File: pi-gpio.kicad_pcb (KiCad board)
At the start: 2 copper layers, 65.1 x 30.1 mm, 15 parts, among them J1 Raspberry_Pi_2_3, J2 printerRelay, J3 UART, J4 uartPower, J5 adxl, J6 powerIn

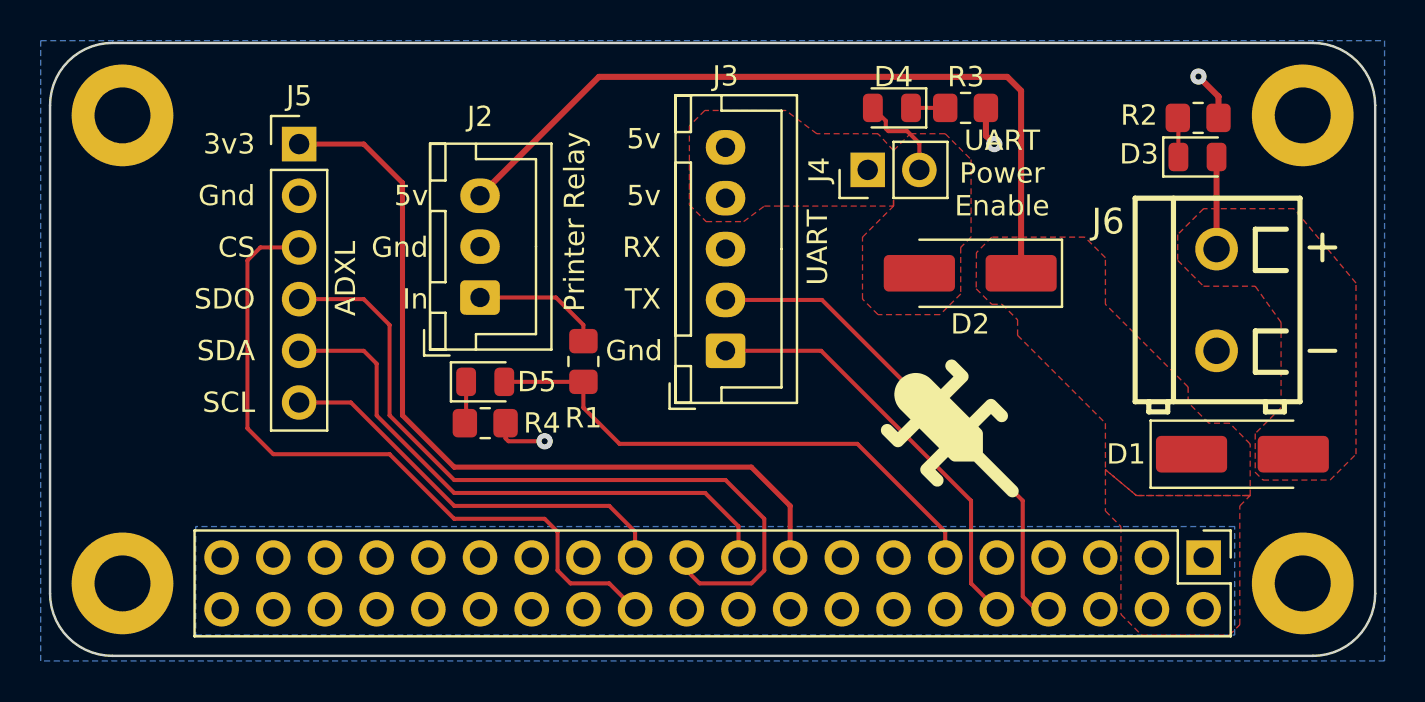
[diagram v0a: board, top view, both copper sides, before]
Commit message: Doubled SPI headers, added I2C
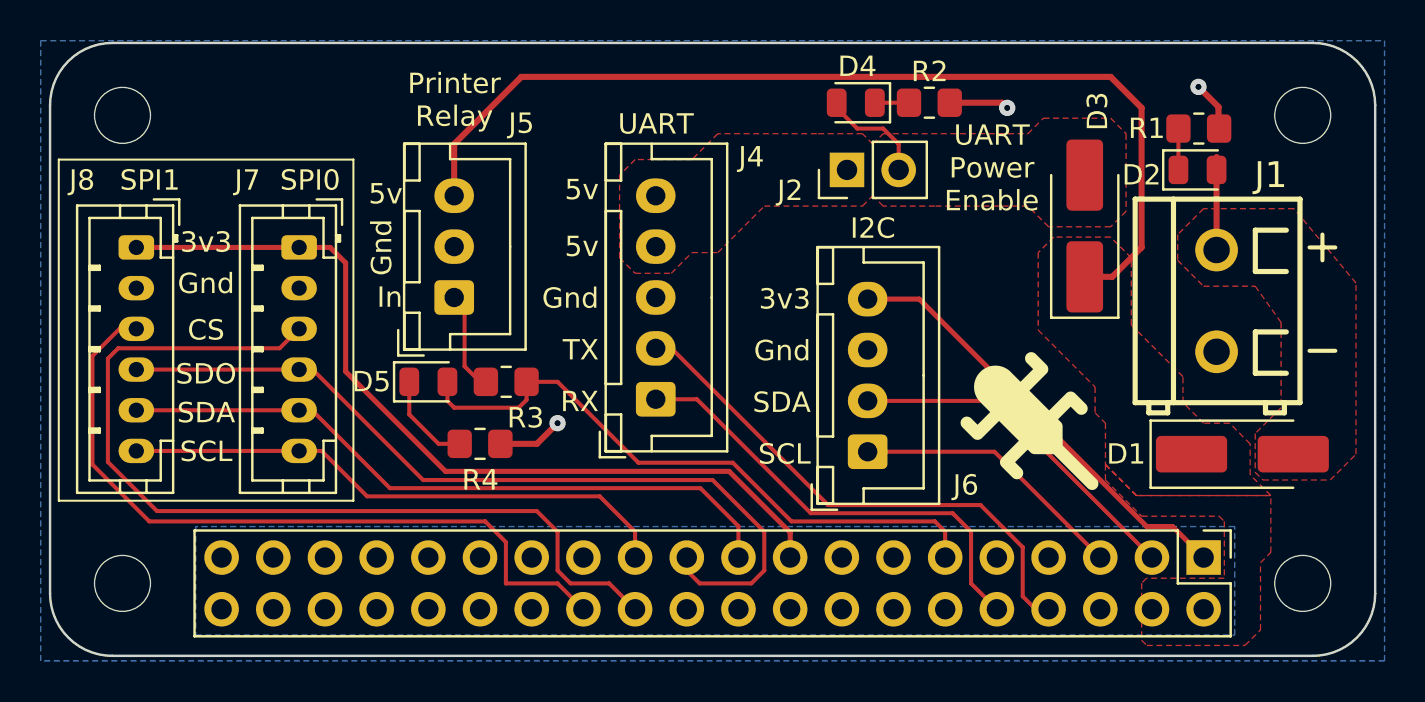
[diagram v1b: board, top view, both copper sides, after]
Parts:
- added J7: SPI0, Connector_JST:JST_PH_B6B-PH-K_1x06_P2.00mm_Vertical, F.Cu at (64.8, 35.6)
- added J8: SPI1, Connector_JST:JST_PH_B6B-PH-K_1x06_P2.00mm_Vertical, F.Cu at (56.8, 35.6)
- D2: value B340A-13-F -> Red; footprint Diode_SMD:D_SMA_Handsoldering -> LED_SMD:LED_0805_2012Metric
- D3: value Red -> B340A-13-F; footprint LED_SMD:LED_0805_2012Metric -> Diode_SMD:D_SMA_Handsoldering
- J1: value Raspberry_Pi_2_3 -> powerIn; footprint jacob-libs:RaspberryPi_Zero_BoardLayout -> jacob-libs:TerminalBlock_MAX_MX127-5.0-02P_1x02_P5.00mm; moved to F.Cu
- J2: value printerRelay -> uartPower; footprint Connector_JST:JST_XH_B3B-XH-A_1x03_P2.50mm_Vertical -> Connector_PinHeader_2.54mm:PinHeader_1x02_P2.54mm_Vertical
- J3: value UART -> Raspberry_Pi_2_3; footprint Connector_JST:JST_XH_B5B-XH-A_1x05_P2.50mm_Vertical -> jacob-libs:RaspberryPi_Zero_BoardLayout; moved to B.Cu
- J4: value uartPower -> UART; footprint Connector_PinHeader_2.54mm:PinHeader_1x02_P2.54mm_Vertical -> Connector_JST:JST_XH_B5B-XH-A_1x05_P2.50mm_Vertical
- J5: value adxl -> printerRelay; footprint Connector_PinHeader_2.54mm:PinHeader_1x06_P2.54mm_Vertical -> Connector_JST:JST_XH_B3B-XH-A_1x03_P2.50mm_Vertical
- J6: value powerIn -> i2c; footprint jacob-libs:TerminalBlock_MAX_MX127-5.0-02P_1x02_P5.00mm -> Connector_JST:JST_XH_B4B-XH-A_1x04_P2.50mm_Vertical
- R1: value 1K -> 150R
- R3: value 150R -> 1K
- moved R1 32.3 mm to (109.0, 29.7), turned to 0 degrees
- moved R3 26.3 mm to (74.9, 42.2)
- moved J3 25.6 mm to (109.2, 50.8)
- moved J2 19.1 mm to (91.7, 31.8)
- moved J6 18.7 mm to (92.7, 45.6)
- moved J4 15.3 mm to (82.3, 43.0)
- moved R2 13.2 mm to (95.7, 28.4)
- moved J1 12.6 mm to (109.9, 38.2)
- moved D2 12.3 mm to (108.9, 31.8), turned to 0 degrees
- moved J5 10.7 mm to (72.4, 38.0), turned to 90 degrees
- moved D3 6.49 mm to (103.4, 34.5), turned to 90 degrees
- moved D5 2.79 mm to (71.1, 42.2)
- moved D4 1.80 mm to (92.1, 28.4)
- moved R4 1.05 mm to (73.7, 45.2)
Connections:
- D2 pad 1: +5V -> Net-(D2-K)
- D2 pad 2: Net-(D2-A) -> Net-(D1-A)
- D3 pad 1: Net-(D3-K) -> +5V
- D3 pad 2: Net-(D1-A) -> Net-(D3-A)
- D4 pad 2: Net-(D2-A) -> Net-(D3-A)
- J1 pad 1: +3V3 -> GND
- J1 pad 2: +5V -> Net-(D1-A)
- J2 pad 2: GND -> Net-(D3-A)
- J3 pad 1: /UART_RXD -> +3V3
- J3 pad 2: /UART_TXD -> +5V
- J3 pad 3: GND -> /I2C_SDA
- J3 pad 4: Net-(J3-Pin_4) -> +5V
- J3 pad 5: Net-(J3-Pin_4) -> /I2C_SCL
- J4 pad 1: Net-(J3-Pin_4) -> /UART_RXD
- J4 pad 2: Net-(D2-A) -> /UART_TXD
- J5 pad 1: +3V3 -> Net-(J5-Pin_1)
- J5 pad 3: /cs_ADXL -> +5V
- J6 pad 1: GND -> /I2C_SCL
- J6 pad 2: Net-(D1-A) -> /I2C_SDA
- R1 pad 1: Net-(J2-Pin_1) -> Net-(D2-K)
- R1 pad 2: /P_RELAY -> GND
- R2 pad 1: Net-(D3-K) -> Net-(D4-K)
- R3 pad 1: Net-(D4-K) -> Net-(J5-Pin_1)
- R3 pad 2: GND -> /P_RELAY
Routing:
- net /SPI_CS0: track 0.00 -> 45.1 mm
- net /SPI_CS1: track 0.00 -> 36.3 mm
- net /cs_ADXL: track 34.9 -> 0.00 mm
- net +3V3: track 40.7 -> 64.1 mm
- net /I2C_SDA: track 0.00 -> 17.2 mm
- net /I2C_SCL: track 0.00 -> 13.6 mm
- net +5V: track 38.3 -> 48.6 mm
- net /SPI_SCLK: track 20.4 -> 27.4 mm
- net Net-(J2-Pin_1): track 6.43 -> 0.00 mm
- net /SPI_MOSI: track 28.2 -> 33.5 mm
- net Net-(J5-Pin_1): track 0.00 -> 5.07 mm
- net Net-(D3-A): track 0.00 -> 5.05 mm
- net Net-(D2-A): track 4.54 -> 0.00 mm
- net /P_RELAY: track 26.7 -> 30.9 mm
- net /SPI_MISO: track 37.9 -> 41.3 mm
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- added copper zone on F.Cu, net Net-(D3-A)
- added copper zone on F.Cu, net Net-(J2-Pin_1)
- removed copper zone on F.Cu, net Net-(D2-A)
- removed copper zone on F.Cu, net Net-(J3-Pin_4)
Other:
- board text added: "I2C"
- board text added: "SPI0"
- board text added: "SPI1"
- board text removed: "ADXL"

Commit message: Added readme
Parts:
- moved D4 0.76 mm to (92.1, 27.7)
- moved R2 0.76 mm to (95.7, 27.7)
- moved D2 0.51 mm to (108.9, 31.2)
- moved R1 0.51 mm to (109.0, 29.2)
- moved D5 0.51 mm to (71.1, 42.7)
- moved R3 0.51 mm to (74.9, 42.7)
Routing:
- net Net-(D3-A): track 5.05 -> 6.07 mm
- net +5V: track 48.6 -> 49.2 mm
- net Net-(J5-Pin_1): track 5.07 -> 5.70 mm
- net Net-(D5-K): track 4.68 -> 4.17 mm
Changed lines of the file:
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@@
 		(legacy_teardrops no)
 	)
-	(paper "A4")
+	(paper "A5")
 	(layers
 		(0 "F.Cu" signal)
@@
 	(footprint "Resistor_SMD:R_0805_2012Metric_Pad1.20x1.40mm_HandSolder"
 		(layer "F.Cu")
-		(at 74.946 42.164)
+		(at 74.946 42.672)
 		(descr "Resistor SMD 0805 (2012 Metric), square (rectangular) end terminal, IPC-7351 nominal with elongated pad for handsoldering. (Body size source: IPC-SM-782 page 72, https://www.pcb-3d.com/wordpress/wp-content/uploads/ipc-sm-782a_amendment_1_and_2.pdf), generated with kicad-footprint-generator")
 		(tags "resistor handsolder")
 		(property "Reference" "R3"
-			(at 0.954 1.778 180)
+			(at 1.762 -1.27 180)
 			(layer "F.SilkS")
 			(effects
@@
 	(footprint "LED_SMD:LED_0805_2012Metric"
 		(layer "F.Cu")
-		(at 71.12 42.164)
+		(at 71.12 42.672)
 		(descr "LED SMD 0805 (2012 Metric), square (rectangular) end terminal, IPC-7351 nominal, (Body size source: https://docs.google.com/spreadsheets/d/1BsfQQcO9C6DZCsRaXUlFlo91Tg2WpOkGARC1WS5S8t0/edit?usp=sharing), generated with kicad-footprint-generator")
 		(tags "LED")
@@
 	(footprint "Resistor_SMD:R_0805_2012Metric_Pad1.20x1.40mm_HandSolder"
 		(layer "F.Cu")
-		(at 95.742 28.448)
+		(at 95.742 27.686)
 		(descr "Resistor SMD 0805 (2012 Metric), square (rectangular) end terminal, IPC-7351 nominal with elongated pad for handsoldering. (Body size source: IPC-SM-782 page 72, https://www.pcb-3d.com/wordpress/wp-content/uploads/ipc-sm-782a_amendment_1_and_2.pdf), generated with kicad-footprint-generator")
 		(tags "resistor handsolder")
 		(property "Reference" "R2"
-			(at 0.016 -1.524 0)
+			(at 2.556 0 0)
 			(layer "F.SilkS")
 			(effects
@@
 	(footprint "LED_SMD:LED_0805_2012Metric"
 		(layer "F.Cu")
-		(at 108.9175 31.75)
+		(at 108.9175 31.242)
 		(descr "LED SMD 0805 (2012 Metric), square (rectangular) end terminal, IPC-7351 nominal, (Body size source: https://docs.google.com/spreadsheets/d/1BsfQQcO9C6DZCsRaXUlFlo91Tg2WpOkGARC1WS5S8t0/edit?usp=sharing), generated with kicad-footprint-generator")
 		(tags "LED")
@@
 	(footprint "LED_SMD:LED_0805_2012Metric"
 		(layer "F.Cu")
-		(at 92.1235 28.448 180)
+		(at 92.1235 27.686 180)
 		(descr "LED SMD 0805 (2012 Metric), square (rectangular) end terminal, IPC-7351 nominal, (Body size source: https://docs.google.com/spreadsheets/d/1BsfQQcO9C6DZCsRaXUlFlo91Tg2WpOkGARC1WS5S8t0/edit?usp=sharing), generated with kicad-footprint-generator")
 		(tags "LED")
 		(property "Reference" "D4"
-			(at -0.0785 1.778 0)
+			(at 2.4615 0 0)
 			(layer "F.SilkS")
 			(effects
@@
 	(footprint "Resistor_SMD:R_0805_2012Metric_Pad1.20x1.40mm_HandSolder"
 		(layer "F.Cu")
-		(at 108.982 29.718)
+		(at 108.982 29.21)
 		(descr "Resistor SMD 0805 (2012 Metric), square (rectangular) end terminal, IPC-7351 nominal with elongated pad for handsoldering. (Body size source: IPC-SM-782 page 72, https://www.pcb-3d.com/wordpress/wp-content/uploads/ipc-sm-782a_amendment_1_and_2.pdf), generated with kicad-footprint-generator")
 		(tags "resistor handsolder")
@@
 	)
 	(segment
-		(start 104.728 37.004)
-		(end 103.378 37.004)
+		(start 76.454 26.416)
+		(end 103.886 26.416)
 		(width 0.3)
 		(layer "F.Cu")
@@
 	)
 	(segment
-		(start 106.172 35.56)
-		(end 104.728 37.004)
+		(start 72.39 30.48)
+		(end 76.454 26.416)
 		(width 0.3)
 		(layer "F.Cu")
@@
 	)
 	(segment
-		(start 104.648 27.178)
-		(end 106.172 28.702)
+		(start 104.728 37.004)
+		(end 103.378 37.004)
 		(width 0.3)
 		(layer "F.Cu")
@@
 	)
 	(segment
-		(start 72.39 30.48)
-		(end 75.692 27.178)
+		(start 103.886 26.416)
+		(end 106.172 28.702)
 		(width 0.3)
 		(layer "F.Cu")
@@
 	)
 	(segment
-		(start 72.39 30.48)
-		(end 72.39 33.02)
+		(start 72.39 33.02)
+		(end 72.39 30.48)
 		(width 0.3)
 		(layer "F.Cu")
@@
 	)
 	(segment
-		(start 75.692 27.178)
-		(end 104.648 27.178)
+		(start 106.172 35.56)
+		(end 104.728 37.004)
 		(width 0.3)
 		(layer "F.Cu")
@@
 	)
 	(segment
-		(start 109.95 29.702)
-		(end 109.95 28.654)
+		(start 109.95 29.194)
+		(end 109.95 28.146)
 		(width 0.3)
 		(layer "F.Cu")
@@
 	)
 	(segment
-		(start 96.742 28.448)
-		(end 99.314 28.448)
+		(start 96.742 27.686)
+		(end 99.314 27.686)
 		(width 0.3)
 		(layer "F.Cu")
@@
 	)
 	(segment
-		(start 109.95 28.654)
-		(end 108.966 27.67)
+		(start 109.95 28.146)
+		(end 108.966 27.162)
 		(width 0.3)
 		(layer "F.Cu")
@@
 	)
 	(segment
-		(start 99.314 28.448)
-		(end 99.568 28.702)
+		(start 99.314 27.686)
+		(end 99.568 27.94)
 		(width 0.3)
 		(layer "F.Cu")
@@
 	)
 	(via
-		(at 99.568 28.702)
+		(at 99.568 27.94)
 		(size 0.8)
 		(drill 0.3)
@@
 	)
 	(via
-		(at 108.966 27.67)
+		(at 108.966 27.162)
 		(size 0.8)
 		(drill 0.3)
@@
 	)
 	(segment
-		(start 72.39 43.434)
-		(end 75.562755 43.434)
+		(start 72.39 43.942)
+		(end 75.562755 43.942)
 		(width 0.2)
 		(layer "F.Cu")
@@
 	)
 	(segment
-		(start 96.52 49.53)
-		(end 96.52 50.8)
+		(start 75.946 42.672)
+		(end 77.978 42.672)
 		(width 0.2)
 		(layer "F.Cu")
@@
 	)
 	(segment
-		(start 72.0575 42.164)
-		(end 72.0575 43.1015)
+		(start 77.978 42.672)
+		(end 81.444 46.138)
 		(width 0.2)
 		(layer "F.Cu")
@@
 	)
 	(segment
-		(start 75.946 43.050755)
-		(end 75.946 42.164)
+		(start 96.52 49.53)
+		(end 96.52 50.8)
 		(width 0.2)
 		(layer "F.Cu")
@@
 	)
 	(segment
-		(start 75.562755 43.434)
-		(end 75.946 43.050755)
+		(start 72.0575 42.672)
+		(end 72.0575 43.6095)
 		(width 0.2)
 		(layer "F.Cu")
@@
 	)
 	(segment
-		(start 96.012 49.022)
-		(end 96.52 49.53)
+		(start 75.946 43.558755)
+		(end 75.946 42.672)
 		(width 0.2)
 		(layer "F.Cu")
@@
 	)
 	(segment
-		(start 72.0575 43.1015)
-		(end 72.39 43.434)
+		(start 75.562755 43.942)
+		(end 75.946 43.558755)
 		(width 0.2)
 		(layer "F.Cu")
@@
 	)
 	(segment
-		(start 81.444 46.138)
-		(end 86.077909 46.138)
+		(start 96.012 49.022)
+		(end 96.52 49.53)
 		(width 0.2)
 		(layer "F.Cu")
@@
 	)
 	(segment
-		(start 77.47 42.164)
-		(end 81.444 46.138)
+		(start 72.0575 43.6095)
+		(end 72.39 43.942)
 		(width 0.2)
 		(layer "F.Cu")
@@
 	)
 	(segment
-		(start 75.946 42.164)
-		(end 77.47 42.164)
+		(start 81.444 46.138)
+		(end 86.077909 46.138)
 		(width 0.2)
 		(layer "F.Cu")
@@
 	)
 	(segment
-		(start 72.66 45.212)
-		(end 71.628 45.212)
+		(start 70.1825 43.7665)
+		(end 70.1825 42.672)
 		(width 0.2)
 		(layer "F.Cu")
@@
 	)
 	(segment
-		(start 70.1825 43.7665)
-		(end 70.1825 42.164)
+		(start 72.66 45.212)
+		(end 71.628 45.212)
 		(width 0.2)
 		(layer "F.Cu")
@@
 	)
 	(segment
-		(start 107.98 31.623)
-		(end 107.98 29.732)
+		(start 107.98 31.115)
+		(end 107.98 29.224)
 		(width 0.2)
 		(layer "F.Cu")
@@
 	)
 	(segment
-		(start 107.98 29.732)
-		(end 107.95 29.702)
+		(start 107.98 29.224)
+		(end 107.95 29.194)
 		(width 0.2)
 		(layer "F.Cu")
@@
 	)
 	(segment
+		(start 91.186 27.686)
+		(end 91.186 28.702)
+		(width 0.2)
+		(layer "F.Cu")
+		(net 15)
+	)
+	(segment
 		(start 94.234 30.48)
 		(end 93.472 29.718)
@@
 	)
 	(segment
-		(start 73.66 42.164)
-		(end 72.898 41.402)
+		(start 72.898 41.624)
+		(end 73.946 42.672)
 		(width 0.2)
 		(layer "F.Cu")
@@
 	)
 	(segment
-		(start 72.898 41.402)
-		(end 72.898 38.528)
+		(start 72.898 38.528)
+		(end 72.898 41.624)
 		(width 0.2)
 		(layer "F.Cu")
@@
 	)
 	(segment
-		(start 73.946 42.164)
-		(end 73.66 42.164)
+		(start 72.39 38.02)
+		(end 72.898 38.528)
 		(width 0.2)
 		(layer "F.Cu")
@@
 	)
 	(segment
-		(start 72.47 38.1)
-		(end 72.39 38.02)
+		(start 73.946 42.164)
+		(end 73.66 42.164)
 		(width 0.2)
 		(layer "F.Cu")
@@
 	)
 	(segment
-		(start 72.898 38.528)
+		(start 72.47 38.1)
 		(end 72.39 38.02)
 		(width 0.2)
@@
 		(fill yes
 			(thermal_gap 0.5)
-			(thermal_bridge_width 1)
+			(thermal_bridge_width 1.5)
 		)
 		(polygon
@@
 				(xy 101.092 39.624) (xy 103.886 42.418) (xy 103.886 43.688) (xy 104.394 44.196) (xy 104.394 46.228)
 				(xy 105.918 47.752) (xy 112.522 47.752) (xy 111.506 46.736) (xy 111.506 45.217928) (xy 110.495861 44.196)
-				(xy 109.22 44.196) (xy 108.204 43.18) (xy 108.204 41.91) (xy 105.664 39.37) (xy 105.664 36.068)
+				(xy 109.22 44.196) (xy 108.204 43.18) (xy 108.204 42.418) (xy 105.664 39.878) (xy 105.664 36.068)
 				(xy 104.648 35.052) (xy 101.854 35.052) (xy 101.092 35.814)
 			)
@@
 		(polygon
 			(pts
-				(xy 115.438 46.99) (xy 116.708 45.72) (xy 116.708 37.3126) (xy 113.66 33.655) (xy 109.215 33.655)
+				(xy 115.692 47.752) (xy 116.708 46.736) (xy 116.708 37.3126) (xy 113.66 33.655) (xy 109.215 33.655)
 				(xy 107.945 34.925) (xy 107.945 36.195) (xy 109.215 37.465) (xy 111.755 37.465) (xy 113.025 39.243)
-				(xy 113.025 43.434) (xy 111.755 44.704) (xy 111.755 46.609) (xy 112.136 46.99)
+				(xy 113.025 43.434) (xy 111.755 44.704) (xy 111.755 46.609) (xy 112.898 47.752)
 			)
 		)
@@
 		(fill yes
 			(thermal_gap 0.5)
-			(thermal_bridge_width 1)
+			(thermal_bridge_width 1.5)
 		)
 		(polygon
